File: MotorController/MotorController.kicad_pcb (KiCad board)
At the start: 2 copper layers, 30.5 x 17.8 mm, 16 parts, among them P1 MOTOR_2, P2 CONN_01X06, U1 L9110, U2 L9110

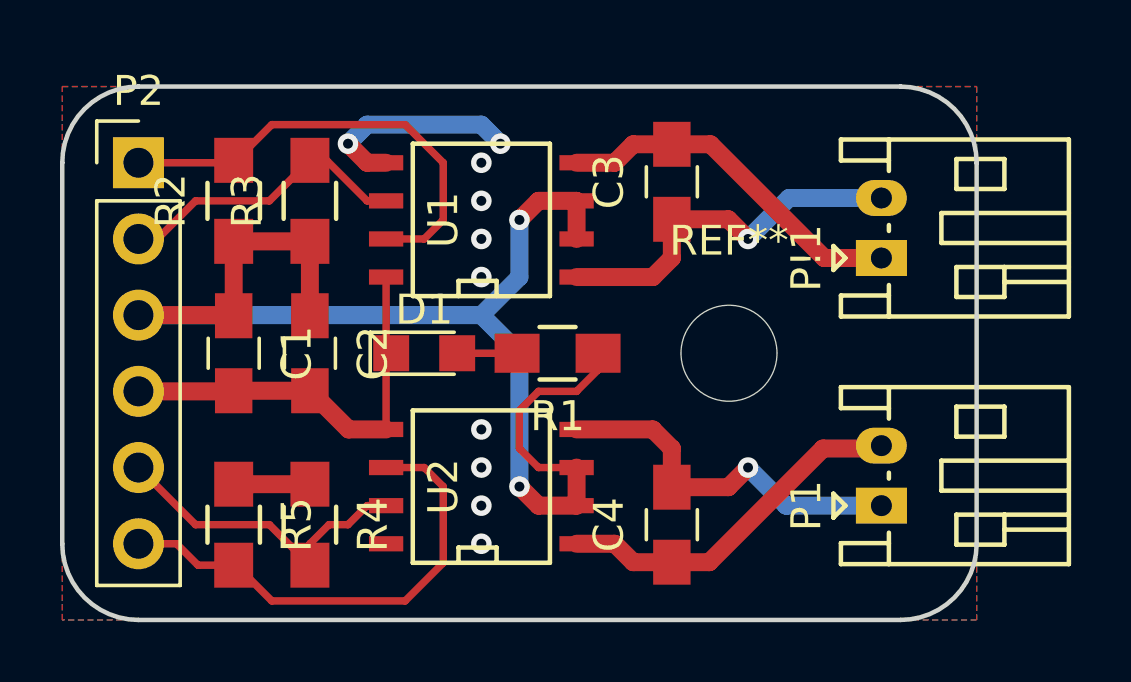
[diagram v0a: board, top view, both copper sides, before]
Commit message: Layout terminado con serigrafia
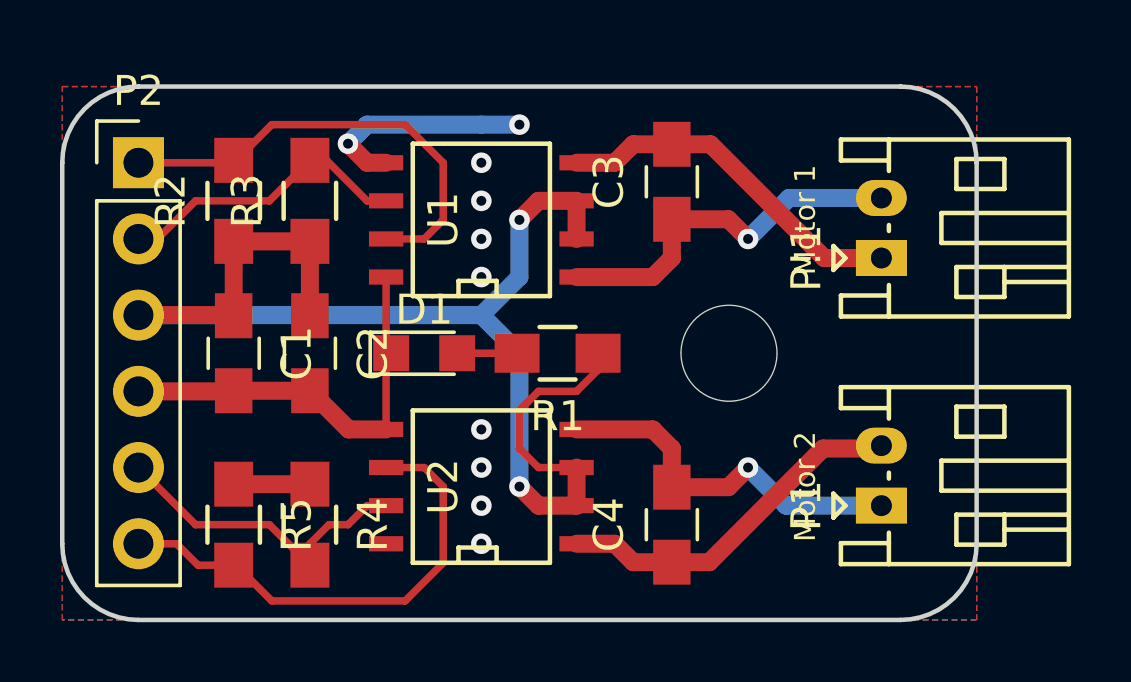
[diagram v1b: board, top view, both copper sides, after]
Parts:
- added G***: LOGO, logos_frizzy:logo_motor_controller, B.Cu at (178.4, 86.4)
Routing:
- net GND: track 22.4 -> 22.8 mm, vias 6 -> 2
- net (no net): vias 4 -> 8
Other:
- board text added: "Motor 1"
- board text added: "Motor 2"
